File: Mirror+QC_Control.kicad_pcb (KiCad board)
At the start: 2 copper layers, 107 x 82 mm, 71 parts, among them J2 Screw_Terminal_01x04, J3 Screw_Terminal_01x06, J4 FSM DRIVER, U1 LT1012, U10 LT1012, U11 LT1012, U2 LM4040DBZ-2.0, U3 LT1012, U5 LT1012, U6 LT1012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

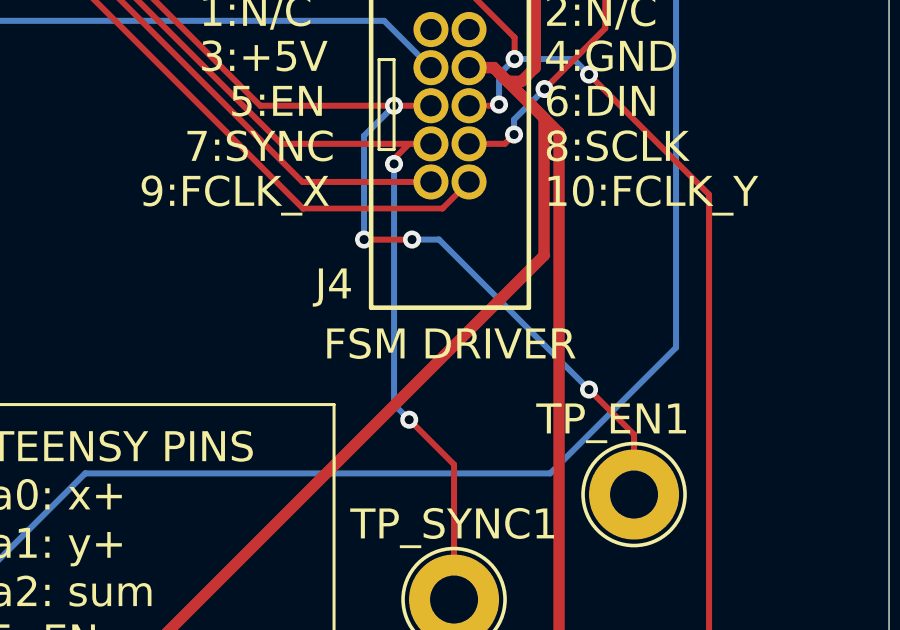
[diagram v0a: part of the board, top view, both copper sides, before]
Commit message: removing fake FSM connector, must solder digikey components
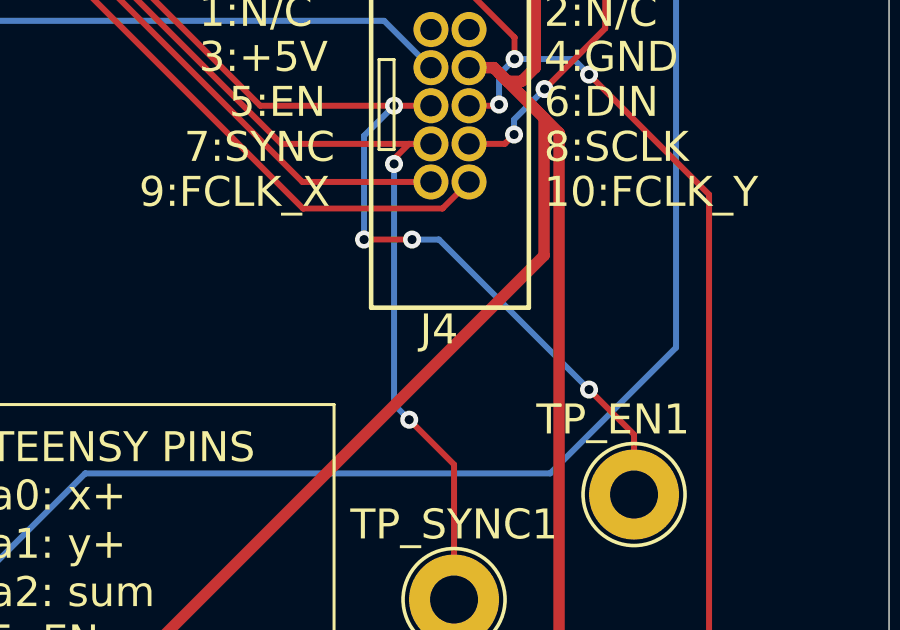
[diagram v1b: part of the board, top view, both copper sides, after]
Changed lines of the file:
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@@
 		(tags "3220-10-0100-00 ")
 		(property "Reference" "J4"
-			(at 8.5 3.23 0)
+			(at 10 -0.27 0)
 			(unlocked yes)
 			(layer "F.SilkS")
@@
 		)
 		(property "Value" "FSM DRIVER"
-			(at 10.5 -0.635 0)
+			(at 2.54 -0.635 270)
 			(unlocked yes)
-			(layer "F.SilkS")
+			(layer "F.Fab")
 			(effects
 				(font
@@
 				(font
 					(size 1.27 1.27)
-					(thickness 0.15)
-				)
-			)
-		)
-		(property "LCSC" "C7501289 "
-			(at 0 0 270)
-			(unlocked yes)
-			(layer "F.Fab")
-			(hide yes)
-			(effects
-				(font
-					(size 1 1)
 					(thickness 0.15)
 				)
@@
 		)
 		(embedded_fonts no)
+		(model "/Users/paigeforester/Downloads/3220-10-0300-00/3220-10-0300-00.step"
+			(offset
+				(xyz 2 1 0)
+			)
+			(scale
+				(xyz 1 1 1)
+			)
+			(rotate
+				(xyz -90 -0 -0)
+			)
+		)
 	)
 	(footprint "DIP THING:CONN8_1-2199298-2_TEC"

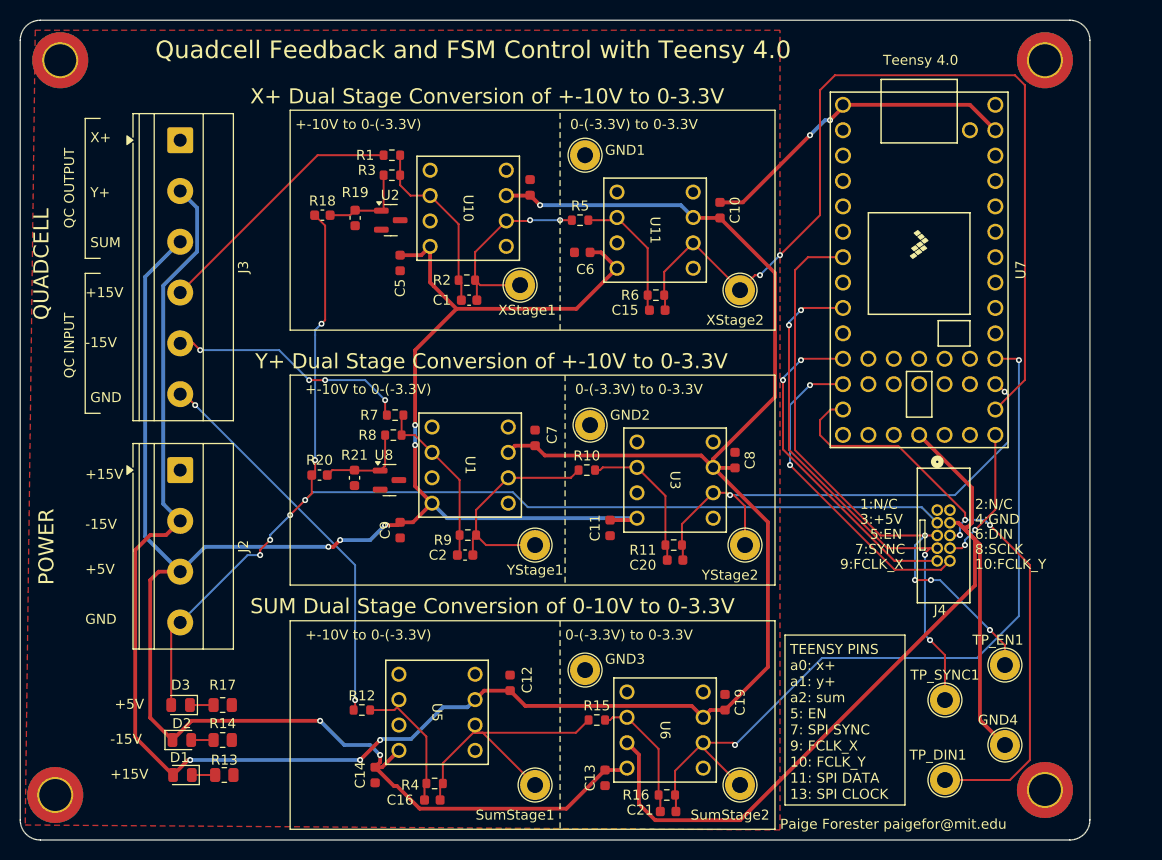
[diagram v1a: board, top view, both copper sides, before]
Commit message: rearranged board for enclosure compatability
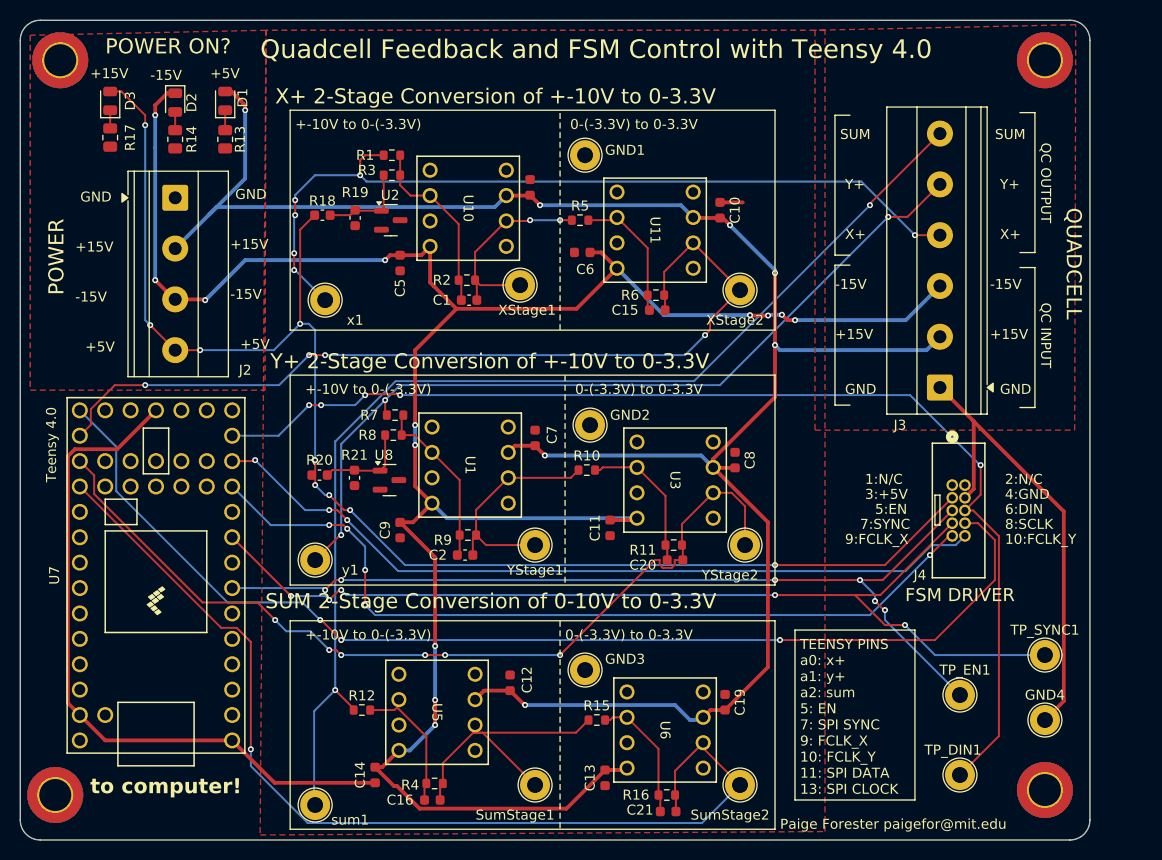
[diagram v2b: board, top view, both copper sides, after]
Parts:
- added sum1: TP_SUM, TestPoint:TestPoint_Loop_D2.60mm_Drill1.6mm_Beaded, F.Cu at (70.0, 103.0)
- added x1: TP_X, TestPoint:TestPoint_Loop_D2.60mm_Drill1.6mm_Beaded, F.Cu at (71.0, 52.5)
- added y1: TP_Y, TestPoint:TestPoint_Loop_D2.60mm_Drill1.6mm_Beaded, F.Cu at (70.0, 78.5)
- moved U7 82.2 mm to (54.1, 80.0), turned to 90 degrees
- moved J3 79.9 mm to (132.5, 61.2), turned to 90 degrees
- moved D1 67.6 mm to (61.0, 32.6), turned to 90 degrees
- moved D2 63.8 mm to (56.0, 32.7), turned to -90 degrees
- moved R13 63.6 mm to (61.0, 36.4), turned to 90 degrees
- moved D3 60.8 mm to (49.5, 32.6), turned to 90 degrees
- moved R14 60.3 mm to (56.0, 36.4), turned to -90 degrees
- moved R17 57.9 mm to (49.5, 36.2), turned to -90 degrees
- moved J2 27.2 mm to (56.0, 42.3)
- moved TP_SYNC1 11.0 mm to (143.0, 88.0)
- moved TP_EN1 5.41 mm to (134.5, 92.0)
- moved GND4 4.72 mm to (143.0, 94.5)
- moved J4 2.92 mm to (133.7, 71.0)
- moved TP_DIN1 1.58 mm to (134.5, 100.0)
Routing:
- net /SCLK: track 13.9 -> 113.8 mm, vias 2 -> 3
- net /sum: track 39.1 -> 114.0 mm
- net /y+: track 24.4 -> 85.0 mm, vias 4 -> 3
- net /x+: track 26.0 -> 83.8 mm, vias 0 -> 6
- net /DIN: track 62.6 -> 114.7 mm, vias 3 -> 5
- net /FCLK_X: track 34.0 -> 84.1 mm, vias 2 -> 5
- net /FCLK_Y: track 32.9 -> 79.4 mm, vias 2 -> 3
- net /SYNC: track 53.9 -> 99.7 mm, vias 4 -> 5
- net /y_stage2: track 52.1 -> 90.3 mm, vias 2 -> 6
- net /EN: track 59.7 -> 91.1 mm, vias 4 -> 6
- net +15V: track 230.4 -> 199.5 mm, vias 4 -> 7
- net /sum_stage2: track 78.9 -> 102.7 mm, vias 2 -> 1
- net +5V: track 121.6 -> 141.7 mm, vias 6 -> 9
- net GND: track 127.8 -> 118.9 mm, vias 2 -> 0
- net -15V: track 217.9 -> 223.4 mm, vias 7 -> 13
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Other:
- board text added: "POWER ON?"
- board text added: "SUM 2-Stage Conversion of 0-10V to 0-3.3V"
- board text added: "X+ 2-Stage Conversion of +-10V to 0-3.3V"
- board text added: "Y+ 2-Stage Conversion of +-10V to 0-3.3V"
- board text added: "to computer!"
- board text removed: "SUM Dual Stage Conversion of 0-10V to 0-3.3V"
- board text removed: "X+ Dual Stage Conversion of +-10V to 0-3.3V"
- board text removed: "Y+ Dual Stage Conversion of +-10V to 0-3.3V"

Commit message: second file for 2QC and 2FSM
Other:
- board text added: "M3"
